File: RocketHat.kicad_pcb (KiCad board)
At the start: 2 copper layers, 68.2 x 58.8 mm, 28 parts, among them J1 Conn_01x06_Female, J10 Conn_01x10_Female, J11 Raspberry_Pi_2_3, J2 Conn_01x06_Female, J3 Conn_01x07_Female, J4 Conn_01x06_Female, J5 Conn_01x04_Female, J6 Conn_01x02_Female, J7 Conn_01x02, J8 Conn_01x10_Female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

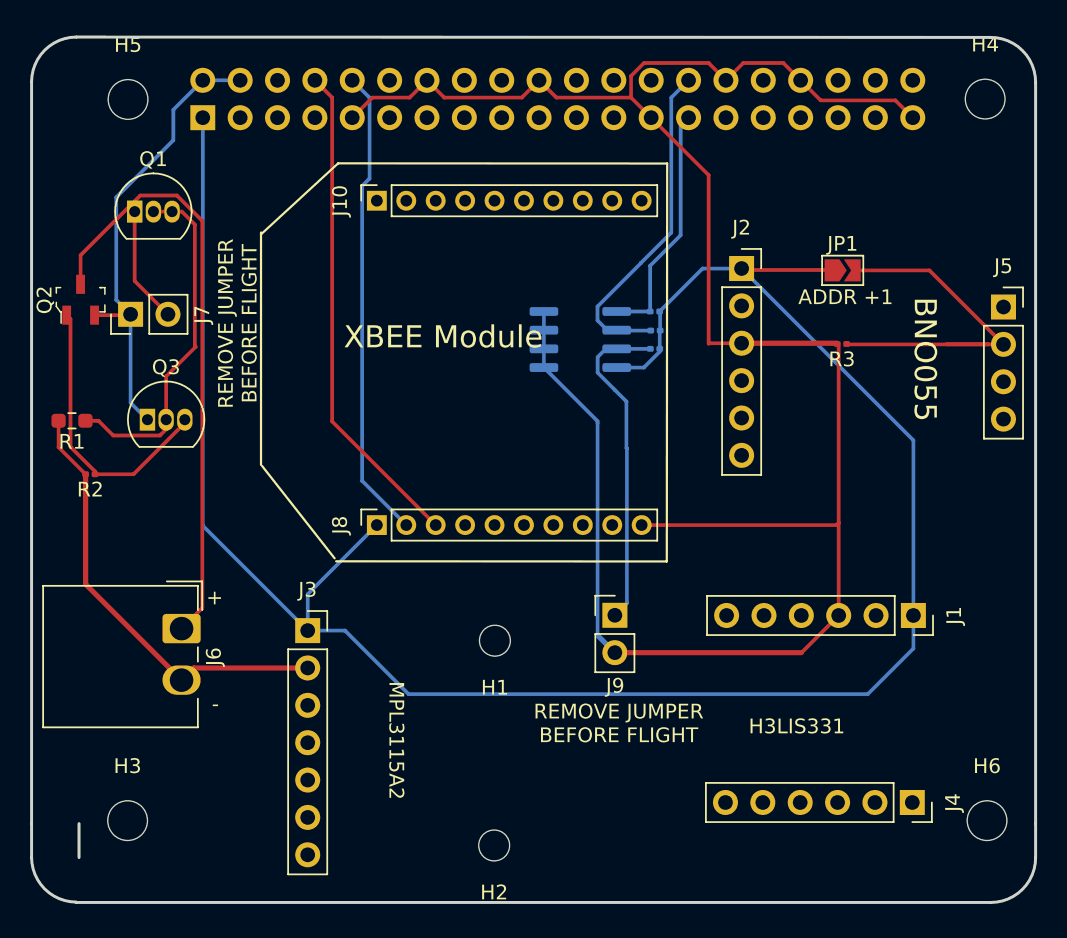
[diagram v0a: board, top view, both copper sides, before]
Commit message: Fixed All DRC Errors
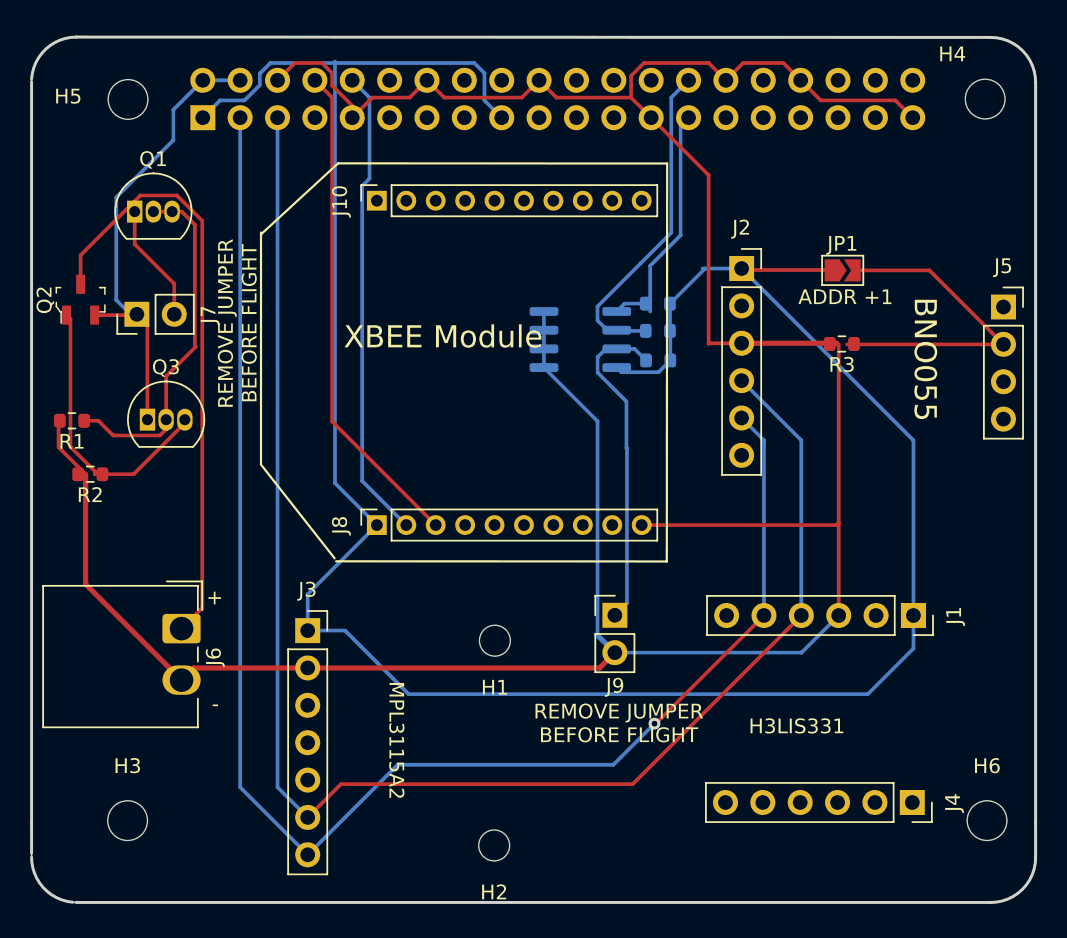
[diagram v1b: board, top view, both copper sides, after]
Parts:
- R1: footprint Resistor_SMD:R_0603_1608Metric_Pad0.98x0.95mm_HandSolder -> Resistor_SMD:R_0603_1608Metric
- R2, R3, R4, R5, R6: footprint Resistor_SMD:R_0201_0603Metric -> Resistor_SMD:R_0603_1608Metric
- moved R4 0.82 mm to (243.5, 115.7)
- moved R5 0.57 mm to (243.4, 111.9)
- moved J7 0.43 mm to (208.0, 112.6)
- moved R6 0.17 mm to (243.4, 113.7)
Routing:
- net /SENSOR_SCL: track 0.00 -> 105.3 mm
- net /SENSOR_SDA: track 0.00 -> 103.8 mm, vias 0 -> 1
- net GND: track 175.8 -> 205.4 mm
- net /3V3: track 141.3 -> 161.7 mm
- net /ADR_BNO055: track 25.8 -> 22.9 mm
- net /P5V_HAT: track 31.4 -> 30.1 mm
- net /EEPROM_SCL: track 22.8 -> 21.7 mm
- net Net-(J9-Pad1): track 22.5 -> 21.8 mm
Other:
- board size 68.2 x 58.8 mm -> 68.3 x 58.8 mm
- board text removed: "0.2000 mm / 0.0000 mm"
- board text removed: "0.3000 mm"
- board text removed: "1.6000 mm"
- board text removed: "68.4498 mm x 59.0264 mm"

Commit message: Fixed Segments
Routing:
- net GND: track 205.4 -> 206.8 mm
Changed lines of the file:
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@@
   (segment (start 255.575544 126.912344) (end 255.727944 126.759944) (width 0.25) (layer "F.Cu") (net 5))
   (segment (start 218.756255 95.506433) (end 217.581744 96.680944) (width 0.25) (layer "F.Cu") (net 5))
+  (segment (start 240.5126 135.5852) (end 237.9472 138.1506) (width 0.35) (layer "F.Cu") (net 5))
   (segment (start 202.697924 121.620364) (end 202.697924 119.825264) (width 0.25) (layer "F.Cu") (net 5))
   (segment (start 249.129 114.554) (end 255.5752 114.554) (width 0.35) (layer "F.Cu") (net 5))
@@
   (segment (start 249.236255 95.506433) (end 251.967233 95.506433) (width 0.25) (layer "F.Cu") (net 5))
   (segment (start 241.616255 97.855455) (end 236.536255 97.855455) (width 0.25) (layer "F.Cu") (net 5))
-  (segment (start 239.4716 136.6262) (end 219.6334 136.6262) (width 0.35) (layer "F.Cu") (net 5))
   (segment (start 242.334544 126.912344) (end 255.575544 126.912344) (width 0.25) (layer "F.Cu") (net 5))
   (segment (start 241.616255 97.855455) (end 241.616255 96.385423) (width 0.25) (layer "F.Cu") (net 5))
@@
   (segment (start 211.886088 136.6262) (end 211.059144 137.453144) (width 0.35) (layer "F.Cu") (net 5))
   (segment (start 253.141744 96.680944) (end 254.507233 98.046433) (width 0.25) (layer "F.Cu") (net 5))
+  (segment (start 219.6334 136.6262) (end 221.2594 138.2522) (width 0.35) (layer "F.Cu") (net 5))
   (segment (start 226.567233 97.855455) (end 224.027233 97.855455) (width 0.25) (layer "F.Cu") (net 5))
   (segment (start 255.5752 114.554) (end 255.624544 114.603344) (width 0.35) (layer "F.Cu") (net 5))
+  (segment (start 237.9472 138.1506) (end 237.9472 138.2522) (width 0.35) (layer "F.Cu") (net 5))
   (segment (start 242.981744 99.220944) (end 246.888 103.1272) (width 0.25) (layer "F.Cu") (net 5))
   (segment (start 227.741744 96.680944) (end 226.567233 97.855455) (width 0.25) (layer "F.Cu") (net 5))
@@
   (segment (start 236.536255 97.855455) (end 235.361744 96.680944) (width 0.25) (layer "F.Cu") (net 5))
   (segment (start 222.661744 99.220944) (end 222.661744 98.404944) (width 0.25) (layer "F.Cu") (net 5))
-  (segment (start 240.5126 135.5852) (end 239.4716 136.6262) (width 0.35) (layer "F.Cu") (net 5))
+  (segment (start 221.2594 138.2522) (end 237.9472 138.2522) (width 0.35) (layer "F.Cu") (net 5))
   (segment (start 241.616255 96.385423) (end 242.495245 95.506433) (width 0.25) (layer "F.Cu") (net 5))
   (segment (start 239.335033 134.433033) (end 239.335033 119.850433) (width 0.25) (layer "B.Cu") (net 5))

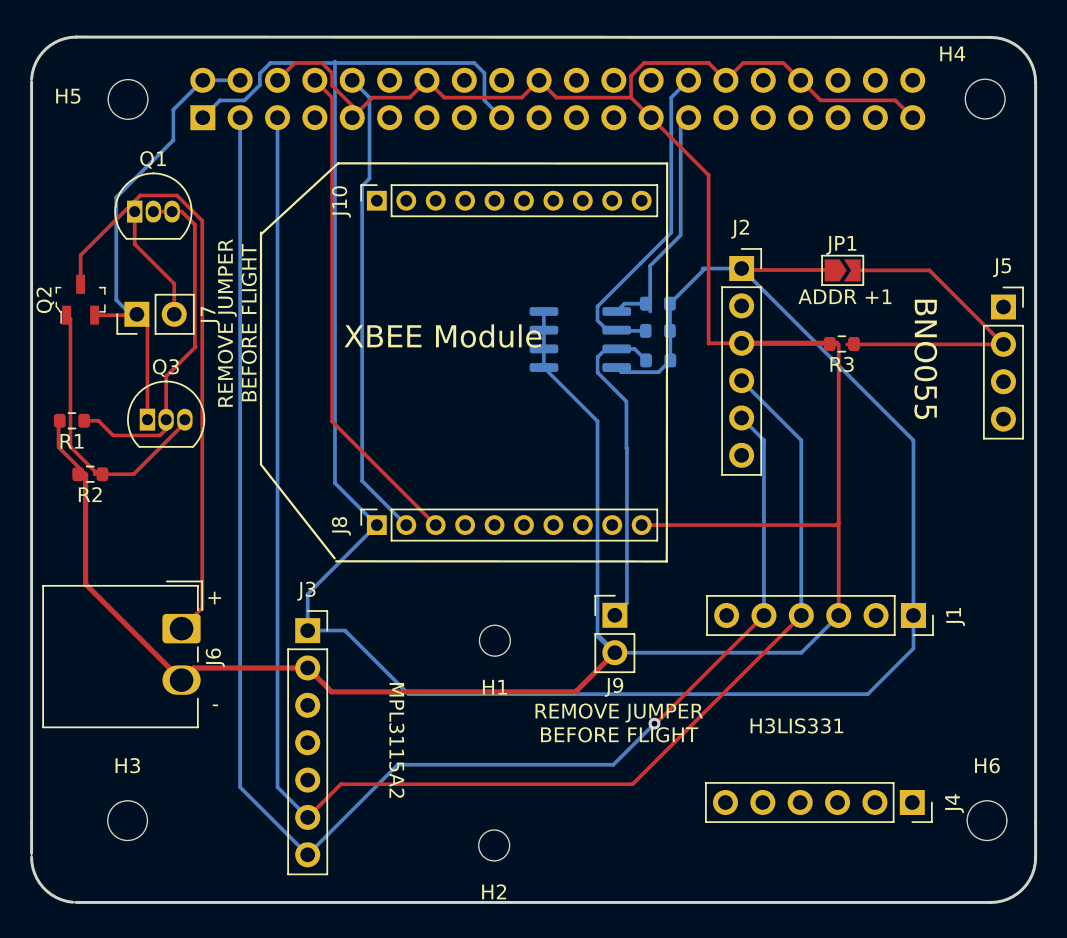
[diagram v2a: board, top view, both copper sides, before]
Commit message: Fixed location of Mounting Holes
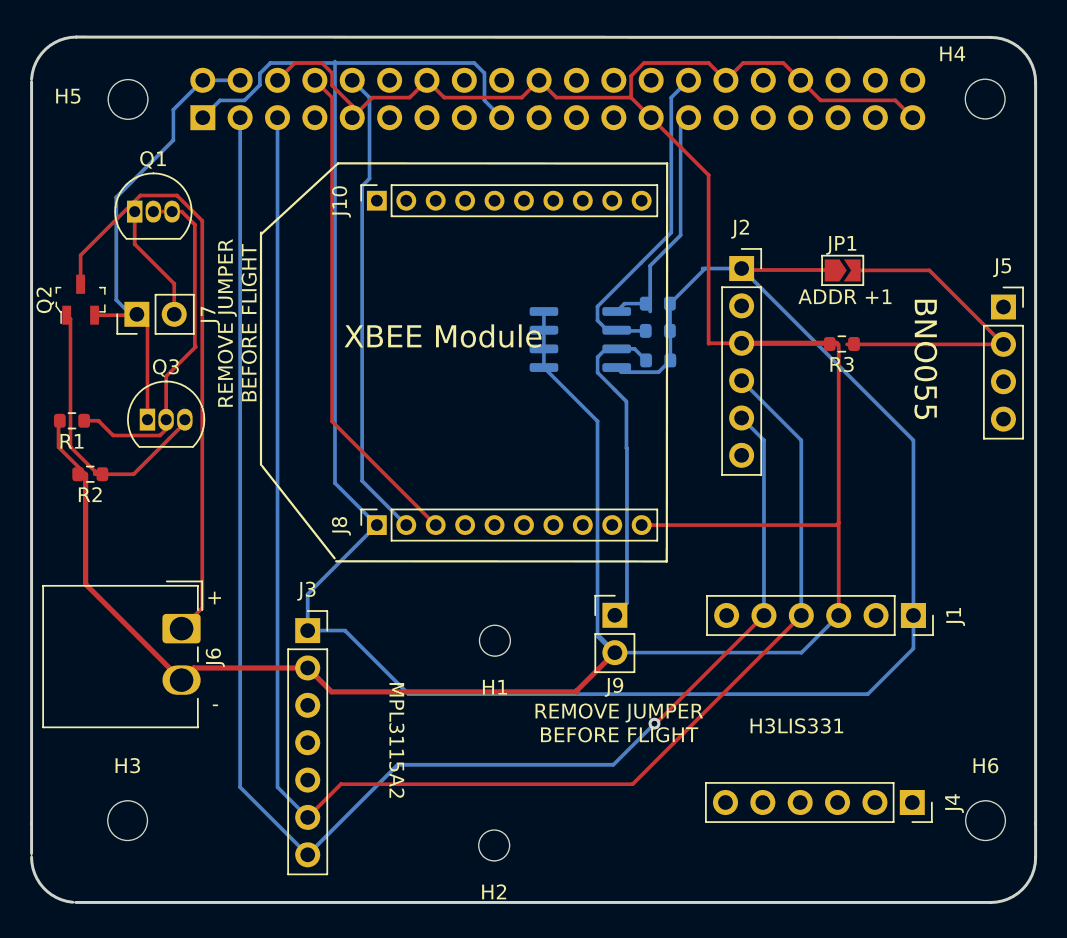
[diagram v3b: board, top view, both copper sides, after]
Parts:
- moved H6 0.10 mm to (265.7, 147.0)
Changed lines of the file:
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@@
   )
   (footprint "MountingHole:MountingHole_2.7mm_M2.5" (layer "F.Cu")
-    (at 265.811744 147.003744)
+    (at 265.7094 147.003744)
     (descr "Mounting Hole 2.7mm, no annular, M2.5")
     (tags "mounting hole 2.7mm no annular m2.5")
@@
   (gr_line (start 216.459544 107.151144) (end 221.701344 102.325144) (layer "F.SilkS") (width 0.15))
   (gr_arc (start 266.065744 93.765344) (mid 268.221005 94.658083) (end 269.113744 96.813344) (layer "Edge.Cuts") (width 0.2))
-  (gr_arc (start 200.863944 96.5962) (mid 201.823374 94.565601) (end 203.911944 93.739944) (layer "Edge.Cuts") (width 0.2))
+  (gr_arc (start 200.863944 96.5962) (mid 201.823373 94.565601) (end 203.911944 93.739944) (layer "Edge.Cuts") (width 0.2))
   (gr_arc (start 269.113744 149.518344) (mid 268.221005 151.673605) (end 266.065744 152.566344) (layer "Edge.Cuts") (width 0.2))
   (gr_line (start 200.863944 96.5962) (end 200.863944 96.787944) (layer "Edge.Cuts") (width 0.1))
